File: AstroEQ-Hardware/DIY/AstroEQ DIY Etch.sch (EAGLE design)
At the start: 40 parts, among them IC1 ATMEGA162-16PU, IC2 PIC18F14K50-I/P, IC3 78L05, J1 POWER_JACKPTH, M1 POLOLU-CARRIER, M2 POLOLU-CARRIER, X1 16MHz, X2 12MHz

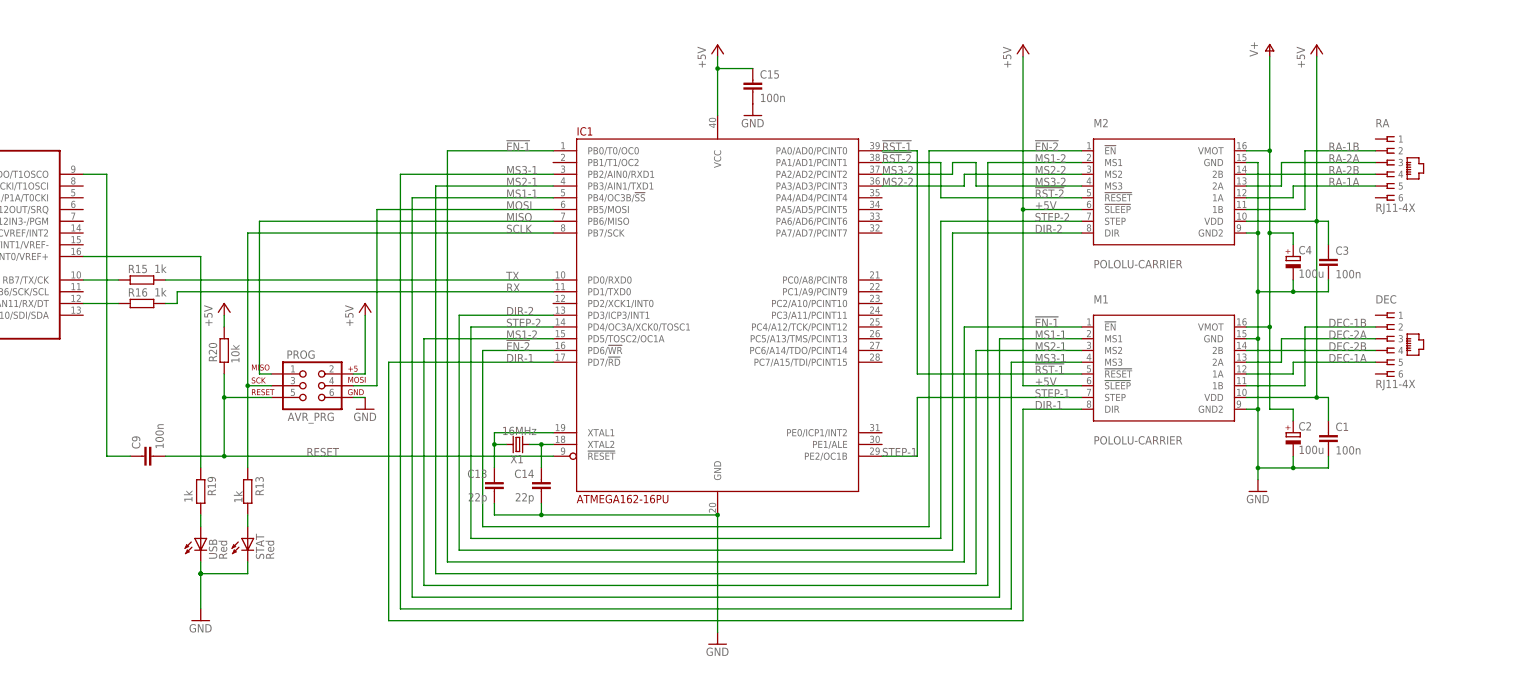
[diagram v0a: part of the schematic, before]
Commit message: Update DIY Eagle Designs
(1) Bring AstroEQ-DIY up to date (V4.4)
(2) Export AstroEQ-DIY schematic to PDF
(3) Make sure the etch file doesn't have holes in pads
(4) Add AstroEQ-ARD variant - Arduino Mega sheild
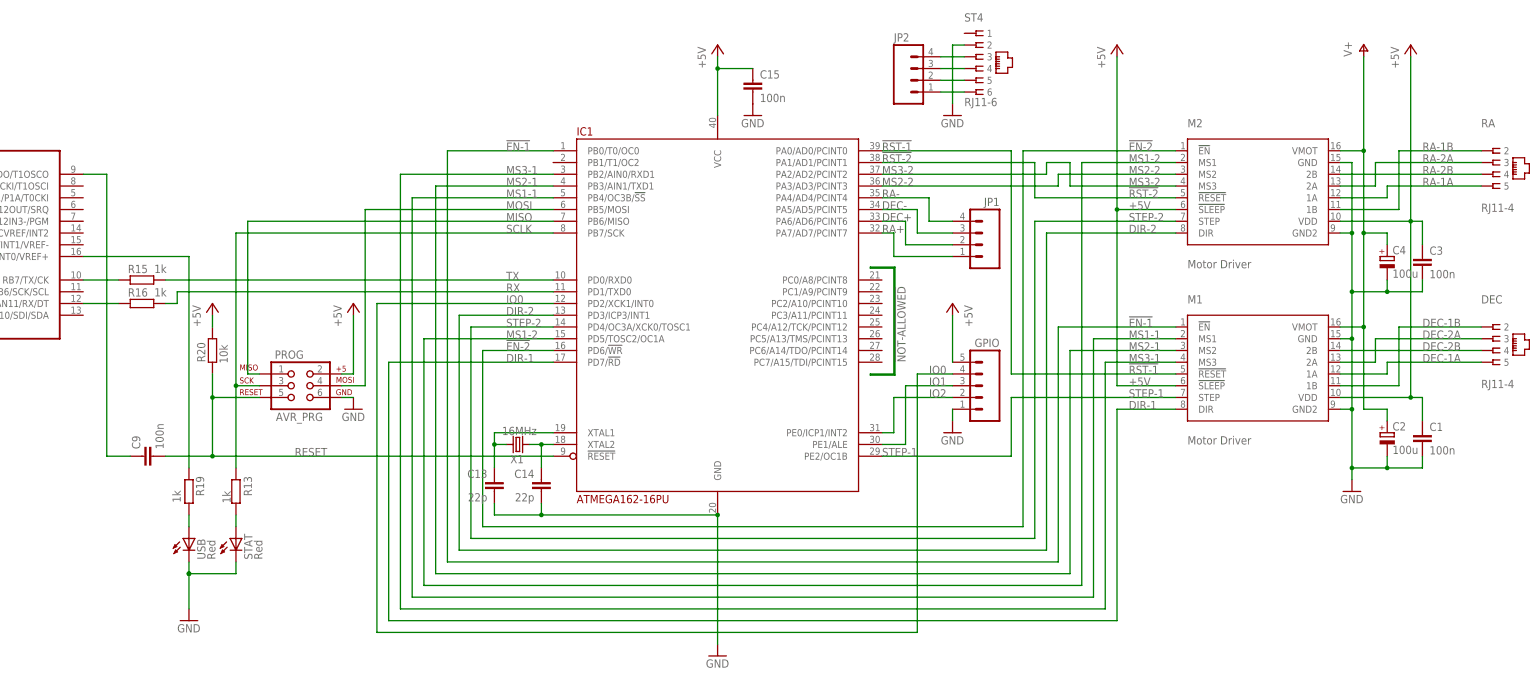
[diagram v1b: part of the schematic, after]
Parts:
- added GPIO: (no value), SparkFun:M05PTH
- added JP1, JP2: (no value), SparkFun:M04PTH
- added ST4: RJ11-6, con-tycoelectronics:RJ11-2L-B
- C13, C14, C6, C7, C8: device rcl:C-EU025-024X044 -> resistor:C-EU025-024X044
- DEC, RA: value RJ11-4X -> RJ11-4; device con-tycoelectronics:RJ11-4X -> con-tycoelectronics:RJ11-4; OC_NEWARK 19R7022 -> (none)
- IC2: MPN PIC18F14K50-I/P -> (none); OC_FARNELL 1648501 -> (none)
- M1, M2: value POLOLU-CARRIER -> Motor Driver
- R15, R16: device SmartPrj:R-EU_0204/7 -> rcl:R-EU_0204/7
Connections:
- new net DEC+: IC1.PA6/AD6/PCINT6, JP1.2
- new net DEC+B: JP2.2, ST4.5
- new net DEC-: IC1.PA5/AD5/PCINT5, JP1.3
- new net DEC-B: JP2.3, ST4.4
- new net IO0: GPIO.4, IC1.PD2/XCK1/INT0
- new net IO1: GPIO.3, IC1.PE1/ALE
- new net IO2: GPIO.2, IC1.PE0/ICP1/INT2
- new net RA+: IC1.PA7/AD7/PCINT7, JP1.1
- new net RA+B: JP2.1, ST4.6
- new net RA-: IC1.PA4/AD4/PCINT4, JP1.4
- new net RA-B: JP2.4, ST4.3
- net +5V: now also GPIO.5
- net GND: now also GPIO.1, ST4.2
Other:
- moved on the sheet: C1, C2, C3, C4, M1, M2, PROG, R13, R19, R20, STAT, USB

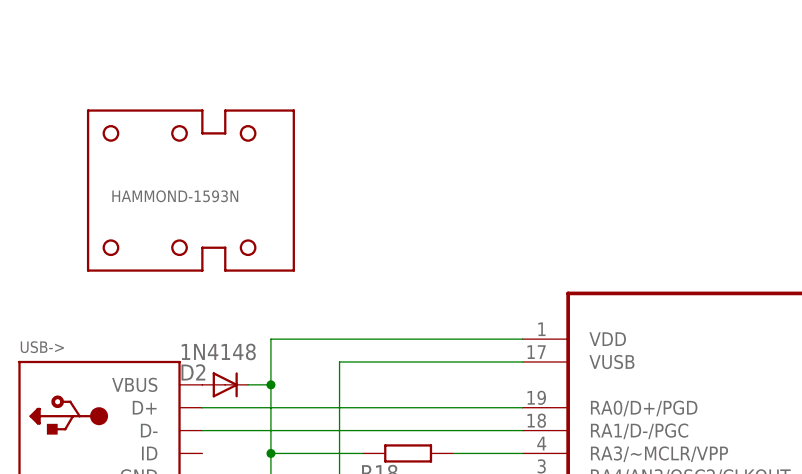
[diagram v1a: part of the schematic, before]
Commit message: Update PCB Logo
Add AstroEQ logo to PCB hardware designs.
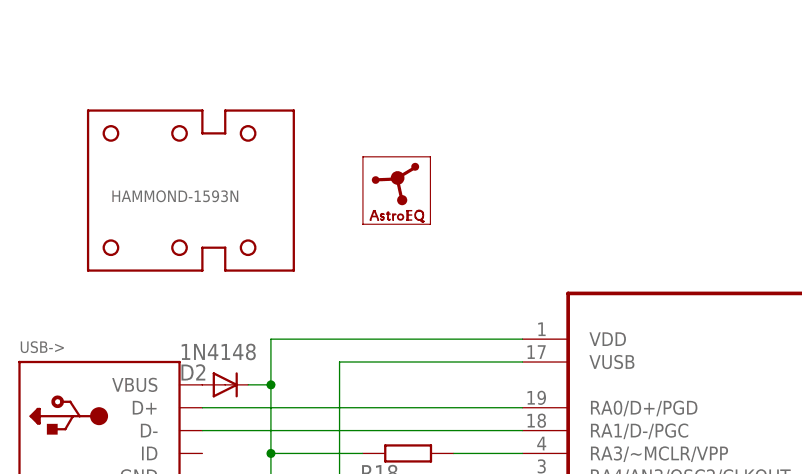
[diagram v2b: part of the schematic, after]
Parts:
- added LOGO1: ASTROEQ3MM, CompanyLogos:ASTROEQ3MM
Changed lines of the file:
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@@
 <layer number="110" name="fp0" color="7" fill="1" visible="no" active="yes"/>
 <layer number="111" name="LPC17xx" color="7" fill="1" visible="yes" active="yes"/>
+<layer number="112" name="tSilk" color="7" fill="1" visible="no" active="yes"/>
 <layer number="116" name="Patch_BOT" color="9" fill="4" visible="no" active="yes"/>
 <layer number="121" name="_tsilk" color="7" fill="1" visible="no" active="yes"/>
@@
 <layer number="124" name="bTestmark" color="7" fill="1" visible="no" active="yes"/>
 <layer number="125" name="_tNames" color="7" fill="1" visible="no" active="yes"/>
+<layer number="126" name="_bNames" color="7" fill="1" visible="no" active="yes"/>
+<layer number="127" name="_tValues" color="7" fill="1" visible="no" active="yes"/>
+<layer number="128" name="_bValues" color="7" fill="1" visible="no" active="yes"/>
 <layer number="131" name="tAdjust" color="7" fill="1" visible="no" active="yes"/>
 <layer number="132" name="bAdjust" color="7" fill="1" visible="no" active="yes"/>
 <layer number="144" name="Drill_legend" color="7" fill="1" visible="no" active="yes"/>
 <layer number="151" name="HeatSink" color="7" fill="1" visible="no" active="yes"/>
+<layer number="152" name="_bDocu" color="7" fill="1" visible="no" active="yes"/>
 <layer number="199" name="Contour" color="7" fill="1" visible="yes" active="yes"/>
 <layer number="200" name="200bmp" color="1" fill="10" visible="no" active="yes"/>
@@
 <layer number="223" name="223bmp" color="24" fill="1" visible="no" active="no"/>
 <layer number="224" name="224bmp" color="25" fill="1" visible="no" active="no"/>
+<layer number="248" name="Housing" color="7" fill="1" visible="no" active="yes"/>
+<layer number="249" name="Edge" color="7" fill="1" visible="no" active="yes"/>
 <layer number="250" name="Descript" color="3" fill="1" visible="no" active="no"/>
 <layer number="251" name="SMDround" color="12" fill="11" visible="no" active="no"/>
@@
 <part name="P+1" library="supply1" deviceset="+5V" device=""/>
 <part name="GND6" library="supply1" deviceset="GND" device=""/>
+<part name="LOGO1" library="CompanyLogos" deviceset="ASTROEQ" device="3MM"/>
 </parts>
 <sheets>
@@
 <instance part="P+1" gate="1" x="312.42" y="213.36" rot="MR0"/>
 <instance part="GND6" gate="1" x="312.42" y="185.42"/>
+<instance part="LOGO1" gate="G$1" x="30.48" y="254"/>
 </instances>
 <busses>

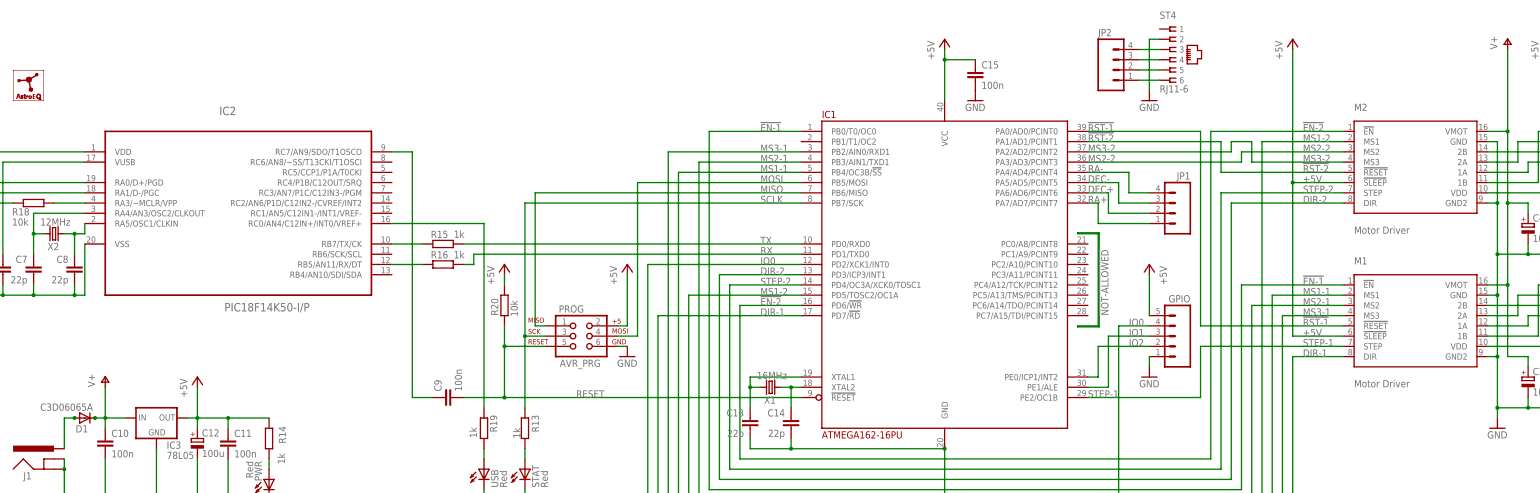
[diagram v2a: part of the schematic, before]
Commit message: Correct Schematic Labelling
Correct labelling in schematic and add additional information to avoid confusion with pin assignments on driver boards.
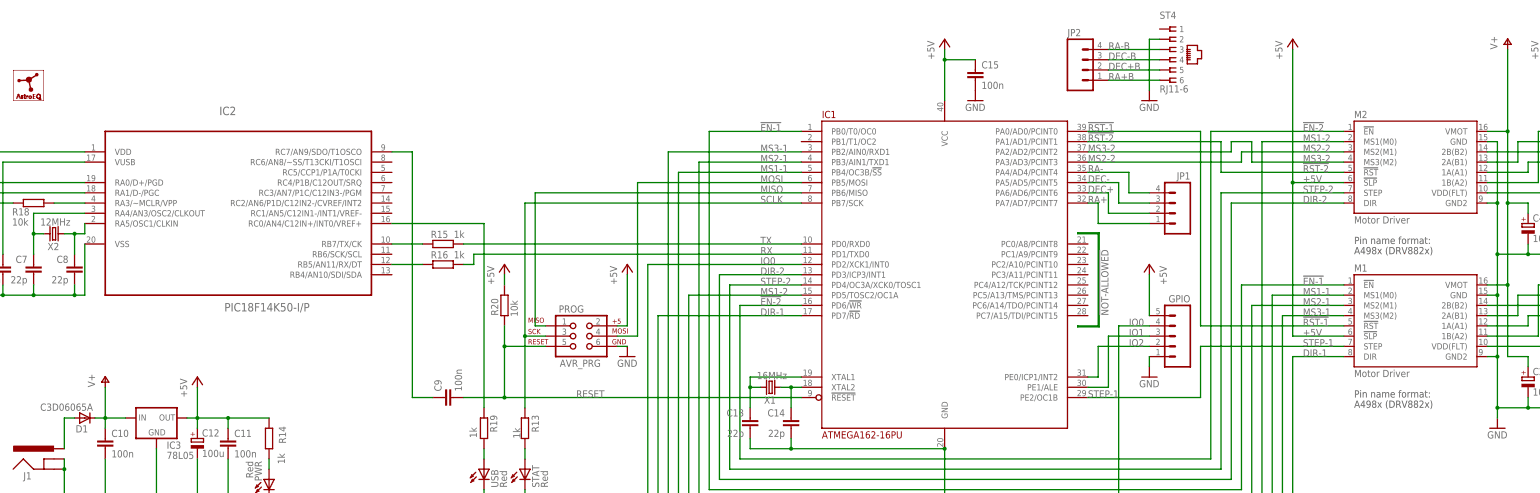
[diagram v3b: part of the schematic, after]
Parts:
- GPIO: MF (none) -> CYNERGY3; MPN (none) -> SSF211X050; OC_FARNELL (none) -> 4249100
- JP1, JP2, LOGO1: OC_FARNELL (none) -> unknown
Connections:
- net !RST-1: now also M1.!RST; no longer M1.!RESET
- net !RST-2: now also M2.!RST; no longer M2.!RESET
- net +5V: now also M1.!SLP, M1.VDD(FLT), M2.!SLP, M2.VDD(FLT); no longer M1.!SLEEP, M1.VDD, M2.!SLEEP, M2.VDD
- net DEC-1A: now also M1.1A(A1); no longer M1.1A
- net DEC-1B: now also M1.1B(A2); no longer M1.1B
- net DEC-2A: now also M1.2A(B1); no longer M1.2A
- net DEC-2B: now also M1.2B(B2); no longer M1.2B
- net MS1-1: now also M1.MS1(M0); no longer M1.MS1
- net MS1-2: now also M2.MS1(M0); no longer M2.MS1
- net MS2-1: now also M1.MS2(M1); no longer M1.MS2
- net MS2-2: now also M2.MS2(M1); no longer M2.MS2
- net MS3-1: now also M1.MS3(M2); no longer M1.MS3
- net MS3-2: now also M2.MS3(M2); no longer M2.MS3
- net RA-1A: now also M2.1A(A1); no longer M2.1A
- net RA-1B: now also M2.1B(A2); no longer M2.1B
- net RA-2A: now also M2.2A(B1); no longer M2.2A
- net RA-2B: now also M2.2B(B2); no longer M2.2B
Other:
- moved on the sheet: JP2
